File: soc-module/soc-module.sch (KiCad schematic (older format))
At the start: 18 parts, among them J1 Micro_SD, J2 East, J3 West, SW1 Prog, SW2 Reset, U1 ATECC608A-SSHDA, U2 ESP32-WROVER-IE-16MB

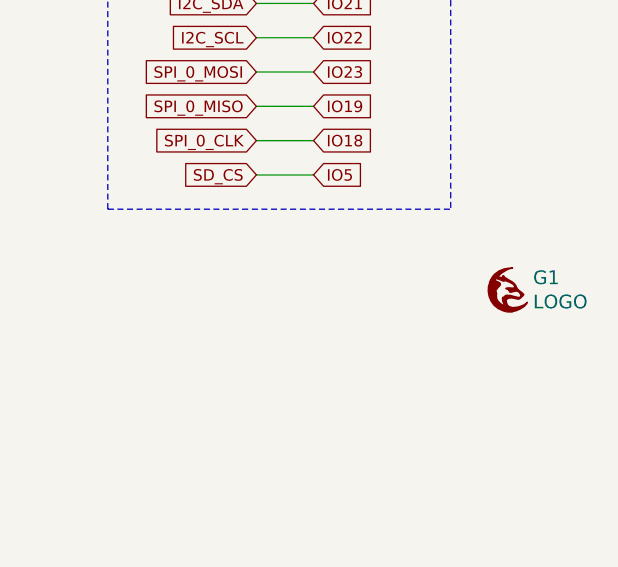
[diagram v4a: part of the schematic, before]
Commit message: Added OpenHardware Logo to PCBs
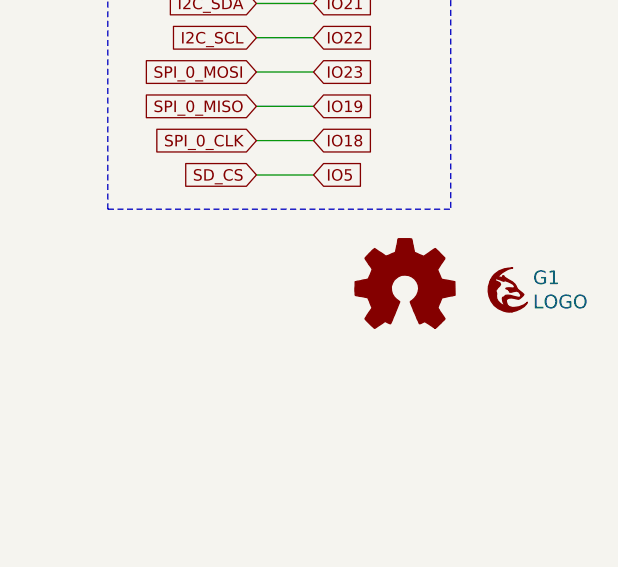
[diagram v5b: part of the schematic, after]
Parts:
- added G2: Logo_Open_Hardware_Small, Symbol:OSHW-Logo2_7.3x6mm_SilkScreen, symbol Graphic:Logo_Open_Hardware_Small
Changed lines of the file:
@@
 Text Notes 2400 5850 0    50   ~ 0
 Buttons
+$Comp
+L Graphic:Logo_Open_Hardware_Small G2
+U 1 1 62527A11
+P 10300 6300
+F 0 "G2" H 10300 6575 50  0001 C CNN
+F 1 "Logo_Open_Hardware_Small" H 10300 6075 50  0001 C CNN
+F 2 "Symbol:OSHW-Logo2_7.3x6mm_SilkScreen" H 10300 6300 50  0001 C CNN
+F 3 "~" H 10300 6300 50  0001 C CNN
+	1    10300 6300
+	1    0    0    -1
+$EndComp
 $EndSCHEMATC
